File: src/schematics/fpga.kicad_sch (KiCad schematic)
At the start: 25 parts

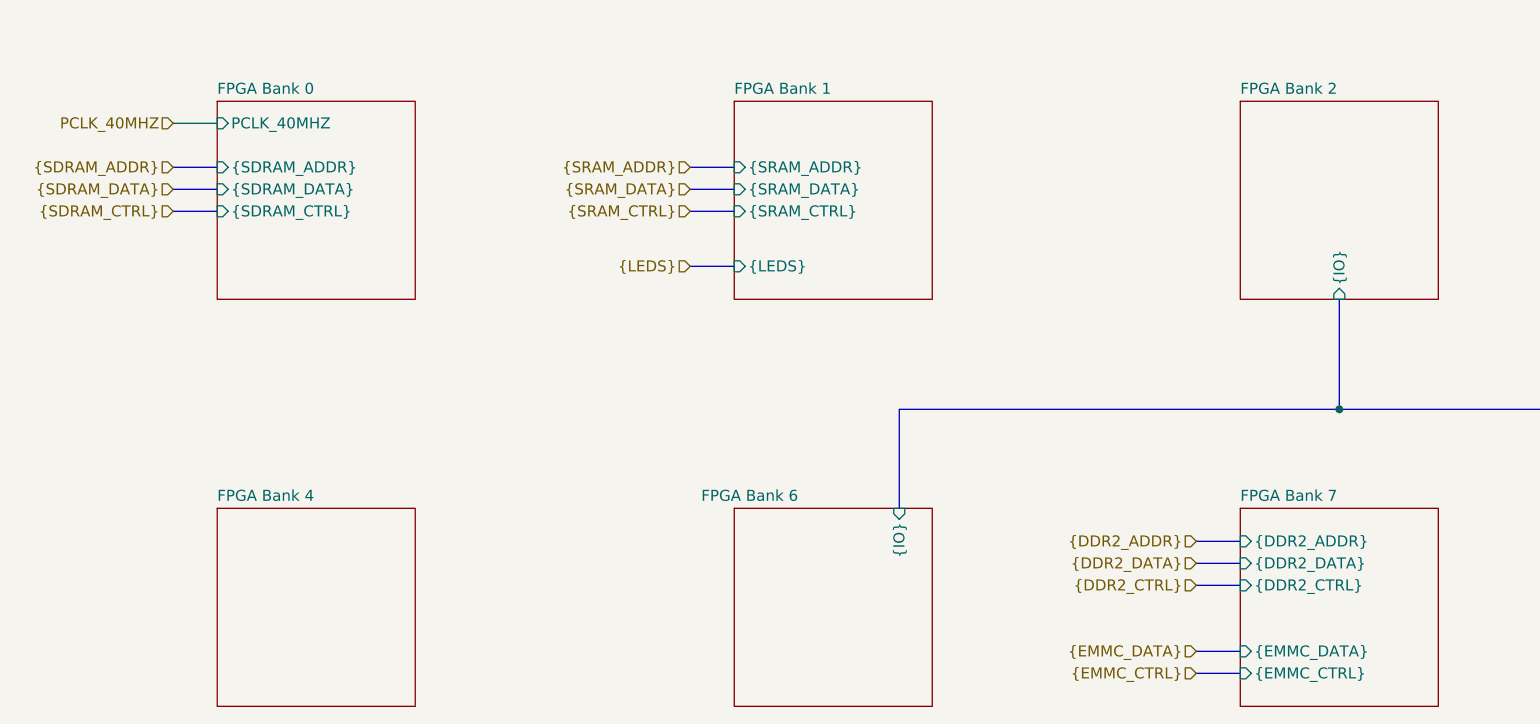
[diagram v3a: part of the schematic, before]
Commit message: Adds bus aliases
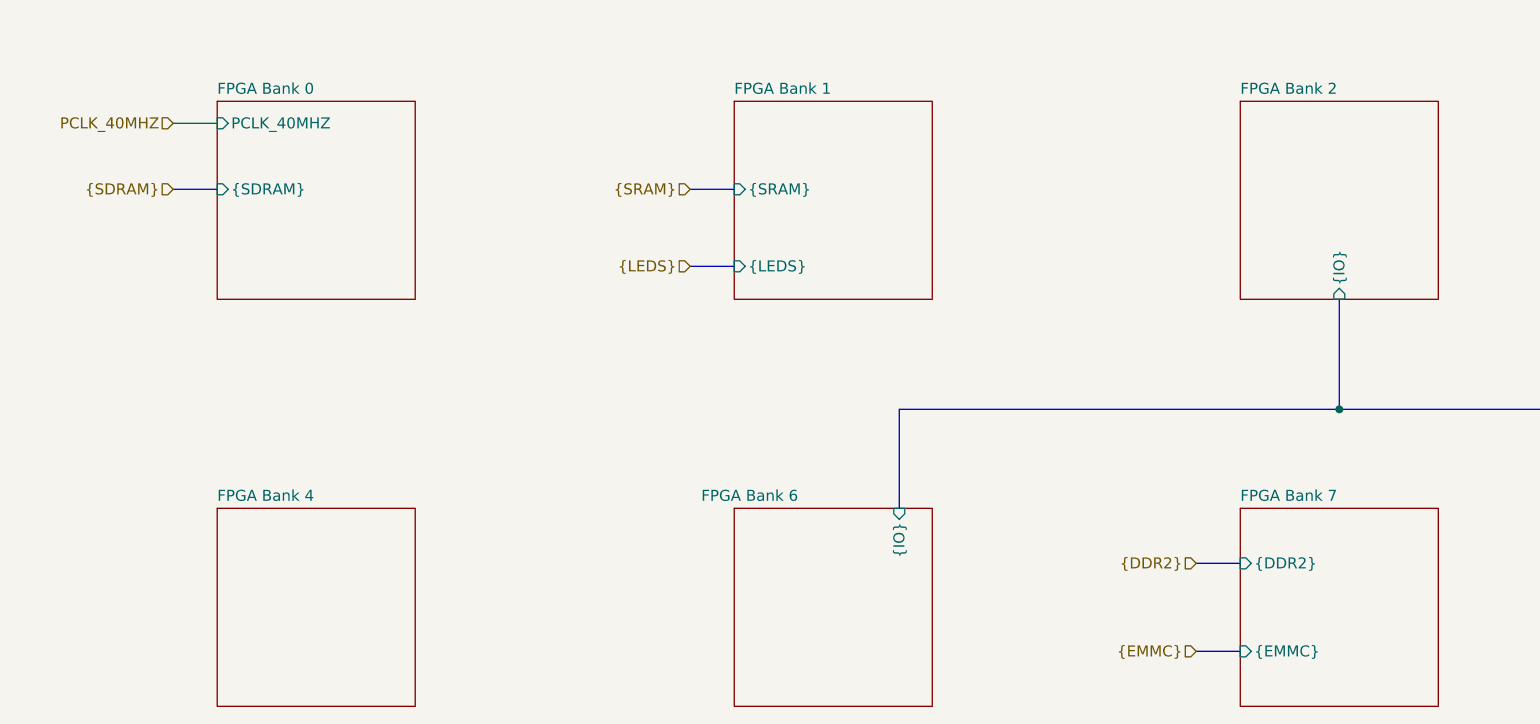
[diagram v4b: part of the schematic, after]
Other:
- sheet FPGA Bank 0 ports: added {SDRAM}; removed {SDRAM_ADDR}, {SDRAM_CTRL}, {SDRAM_DATA}
- sheet FPGA Bank 1 ports: added {SRAM}; removed {SRAM_ADDR}, {SRAM_CTRL}, {SRAM_DATA}
- sheet FPGA Bank 7 ports: added {DDR2}, {EMMC}; removed {DDR2_ADDR}, {DDR2_CTRL}, {DDR2_DATA}, {EMMC_CTRL}, {EMMC_DATA}
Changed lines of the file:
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@@
 		(rev "${Revision}")
 		(comment 1 "${Project Title}")
-		(comment 2 "FPGA POWER")
+		(comment 2 "FPGA")
 		(comment 3 "${Part Number}")
 	)
@@
 	(bus
 		(pts
-			(xy 40.64 91.44) (xy 45.72 91.44)
-		)
-		(stroke
-			(width 0)
-			(type default)
-		)
-	)
-	(bus
-		(pts
-			(xy 158.75 149.86) (xy 163.83 149.86)
-		)
-		(stroke
-			(width 0)
-			(type default)
-		)
-	)
-	(bus
-		(pts
 			(xy 100.33 93.98) (xy 105.41 93.98)
 		)
@@
 		)
 	)
-	(bus
-		(pts
-			(xy 158.75 134.62) (xy 163.83 134.62)
-		)
-		(stroke
-			(width 0)
-			(type default)
-		)
-	)
 	(wire
 		(pts
@@
 		)
 	)
-	(bus
-		(pts
-			(xy 100.33 96.52) (xy 105.41 96.52)
-		)
-		(stroke
-			(width 0)
-			(type default)
-		)
-	)
 	(wire
 		(pts
@@
 		)
 	)
-	(bus
-		(pts
-			(xy 100.33 91.44) (xy 105.41 91.44)
-		)
-		(stroke
-			(width 0)
-			(type default)
-		)
-	)
 	(wire
 		(pts
@@
 		)
 	)
-	(bus
-		(pts
-			(xy 158.75 139.7) (xy 163.83 139.7)
-		)
-		(stroke
-			(width 0)
-			(type default)
-		)
-	)
 	(wire
 		(pts
@@
 		)
 	)
-	(bus
-		(pts
-			(xy 40.64 96.52) (xy 45.72 96.52)
-		)
-		(stroke
-			(width 0)
-			(type default)
-		)
-	)
 	(wire
 		(pts
@@
 		)
 	)
-	(hierarchical_label "{SDRAM_CTRL}"
-		(shape input)
-		(at 40.64 96.52 180)
-		(fields_autoplaced yes)
-		(effects
-			(font
-				(size 1.27 1.27)
-			)
-			(justify right)
-		)
-	)
-	(hierarchical_label "{DDR2_CTRL}"
-		(shape input)
-		(at 158.75 139.7 180)
-		(fields_autoplaced yes)
-		(effects
-			(font
-				(size 1.27 1.27)
-			)
-			(justify right)
-		)
-	)
-	(hierarchical_label "{SDRAM_DATA}"
+	(hierarchical_label "{SDRAM}"
 		(shape input)
 		(at 40.64 93.98 180)
@@
 		)
 	)
-	(hierarchical_label "{SDRAM_ADDR}"
-		(shape input)
-		(at 40.64 91.44 180)
-		(fields_autoplaced yes)
-		(effects
-			(font
-				(size 1.27 1.27)
-			)
-			(justify right)
-		)
-	)
-	(hierarchical_label "{SRAM_ADDR}"
-		(shape input)
-		(at 100.33 91.44 180)
-		(fields_autoplaced yes)
-		(effects
-			(font
-				(size 1.27 1.27)
-			)
-			(justify right)
-		)
-	)
-	(hierarchical_label "{SRAM_DATA}"
+	(hierarchical_label "{SRAM}"
 		(shape input)
 		(at 100.33 93.98 180)
@@
 		)
 	)
-	(hierarchical_label "{SRAM_CTRL}"
-		(shape input)
-		(at 100.33 96.52 180)
-		(fields_autoplaced yes)
-		(effects
-			(font
-				(size 1.27 1.27)
-			)
-			(justify right)
-		)
-	)
-	(hierarchical_label "{EMMC_DATA}"
+	(hierarchical_label "{EMMC}"
 		(shape input)
 		(at 158.75 147.32 180)
@@
 		)
 	)
-	(hierarchical_label "{DDR2_ADDR}"
-		(shape input)
-		(at 158.75 134.62 180)
-		(fields_autoplaced yes)
-		(effects
-			(font
-				(size 1.27 1.27)
-			)
-			(justify right)
-		)
-	)
-	(hierarchical_label "{EMMC_CTRL}"
-		(shape input)
-		(at 158.75 149.86 180)
-		(fields_autoplaced yes)
-		(effects
-			(font
-				(size 1.27 1.27)
-			)
-			(justify right)
-		)
-	)
 	(hierarchical_label "{LEDS}"
 		(shape input)
@@
 		)
 	)
-	(hierarchical_label "{DDR2_DATA}"
+	(hierarchical_label "{DDR2}"
 		(shape input)
 		(at 158.75 137.16 180)
@@
 			)
 		)
-		(pin "{SRAM_CTRL}" input
-			(at 105.41 96.52 180)
-			(effects
-				(font
-					(size 1.27 1.27)
-				)
-				(justify left)
-			)
-		)
-		(pin "{SRAM_ADDR}" input
-			(at 105.41 91.44 180)
-			(effects
-				(font
-					(size 1.27 1.27)
-				)
-				(justify left)
-			)
-		)
-		(pin "{SRAM_DATA}" input
+		(pin "{SRAM}" input
 			(at 105.41 93.98 180)
 			(effects
@@
 			)
 		)
-		(pin "{EMMC_DATA}" input
+		(pin "{EMMC}" input
 			(at 163.83 147.32 180)
 			(effects
@@
 			)
 		)
-		(pin "{EMMC_CTRL}" input
-			(at 163.83 149.86 180)
-			(effects
-				(font
-					(size 1.27 1.27)
-				)
-				(justify left)
-			)
-		)
-		(pin "{DDR2_DATA}" input
+		(pin "{DDR2}" input
 			(at 163.83 137.16 180)
 			(effects
@@
 			)
 		)
-		(pin "{DDR2_ADDR}" input
-			(at 163.83 134.62 180)
-			(effects
-				(font
-					(size 1.27 1.27)
-				)
-				(justify left)
-			)
-		)
-		(pin "{DDR2_CTRL}" input
-			(at 163.83 139.7 180)
-			(effects
-				(font
-					(size 1.27 1.27)
-				)
-				(justify left)
-			)
-		)
 		(instances
 			(project "ecap5-bsom"
@@
 			)
 		)
-		(pin "{SDRAM_DATA}" input
+		(pin "{SDRAM}" input
 			(at 45.72 93.98 180)
 			(effects
 				(font
-					(size 1.27 1.27)
-				)
-				(justify left)
-			)
-		)
-		(pin "{SDRAM_CTRL}" input
-			(at 45.72 96.52 180)
-			(effects
-				(font
-					(size 1.27 1.27)
-				)
-				(justify left)
-			)
-		)
-		(pin "{SDRAM_ADDR}" input
-			(at 45.72 91.44 180)
-			(effects
-				(font

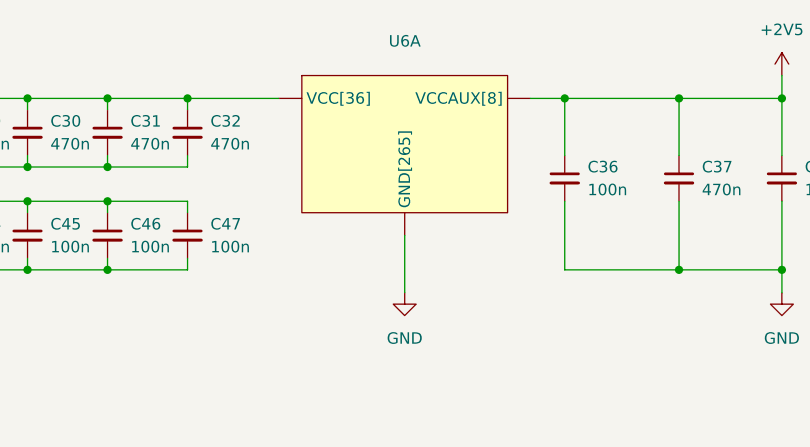
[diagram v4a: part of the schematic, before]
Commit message: Fix some ERC issues
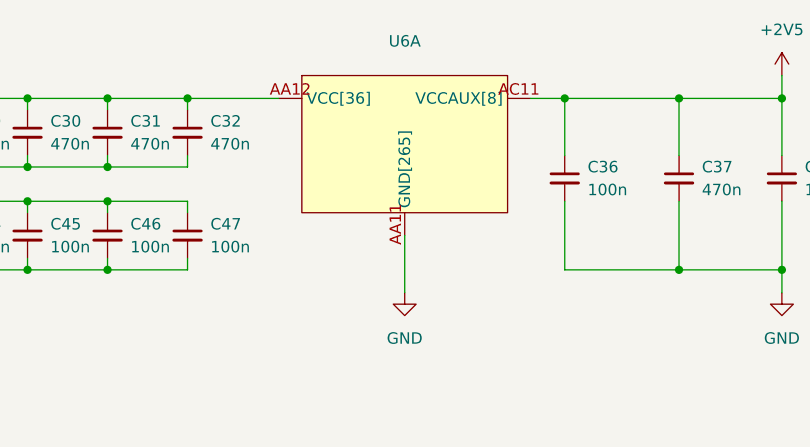
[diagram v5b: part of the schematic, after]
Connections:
- net +1V1: no longer U6. (VCC[36])
- net +2V5: no longer U6. (VCC[36])
- net GND: no longer U6. (VCC[36])
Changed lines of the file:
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@@
 			)
 		)
-		(pin ""
-		)
-		(pin ""
-		)
-		(pin ""
-		)
 		(pin "AA11"
 		)
@@
 		(pin "Y31"
 		)
-		(pin ""
-		)
 		(pin "A10"
 		)
@@
 		(pin "K16"
 		)
-		(pin ""
-		)
 		(pin "A18"
 		)
@@
 		(pin "K21"
 		)
-		(pin ""
-		)
 		(pin "B32"
 		)
@@
 		(pin "T23"
 		)
-		(pin ""
-		)
 		(pin "AA23"
 		)
@@
 		(pin "Y32"
 		)
-		(pin ""
-		)
 		(pin "AB23"
 		)
@@
 		(pin "AM31"
 		)
-		(pin ""
-		)
 		(pin "AA10"
 		)
@@
 		(pin "Y7"
 		)
-		(pin ""
-		)
 		(pin "B1"
 		)
@@
 		(pin "T10"
 		)
-		(pin ""
-		)
 		(pin "AB10"
